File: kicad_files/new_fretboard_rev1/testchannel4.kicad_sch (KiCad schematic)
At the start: 22 parts, among them U2 LX3302AQPW-TR-EASY

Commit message: got 6 of em
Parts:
- removed C12, C13: 680pf, Capacitor_SMD:C_0603_1608Metric, symbol Device:C
- removed C14, C15: 10pf, Capacitor_SMD:C_0402_1005Metric, symbol Device:C
- removed C16: 1uf, Capacitor_SMD:C_0603_1608Metric, symbol Device:C
- removed C17, C20: 100nf, Capacitor_SMD:C_0402_1005Metric, symbol Device:C
- removed C18, C19: 6.8nf, Capacitor_SMD:C_0402_1005Metric, symbol Device:C
- removed C21: 1000pf, Capacitor_SMD:C_0402_1005Metric, symbol Device:C
- removed C22: 470nf, Capacitor_SMD:C_0402_1005Metric, symbol Device:C
- removed L5, L6, L7, L8: L, NetTie:NetTie-2_SMD_Pad0.5mm, symbol Device:L
- removed R10, R11, R8, R9: 10R, Resistor_SMD:R_0402_1005Metric, symbol Device:R
- removed R12: 221R, Resistor_SMD:R_0402_1005Metric, symbol Device:R
- removed R13: 4.7R, Resistor_SMD:R_0402_1005Metric, symbol Device:R
- removed U2: LX3302AQPW-TR-EASY, Snapeda:14-TSSOP_MCH-L, symbol Snapeda:LX3302AQPW-TR-EASY
- added C45, C51: 100nf, Capacitor_SMD:C_0402_1005Metric, symbol Device:C
- added C46: 1000pf, Capacitor_SMD:C_0402_1005Metric, symbol Device:C
- added C47: 470nf, Capacitor_SMD:C_0402_1005Metric, symbol Device:C
- added C48: 1uf, Capacitor_SMD:C_0603_1608Metric, symbol Device:C
- added C49, C50: 6.8nf, Capacitor_SMD:C_0402_1005Metric, symbol Device:C
- added C52, C53: 10pf, Capacitor_SMD:C_0402_1005Metric, symbol Device:C
- added C54, C55: 680pf, Capacitor_SMD:C_0603_1608Metric, symbol Device:C
- added L17, L18, L19, L20: L, NetTie:NetTie-2_SMD_Pad0.5mm, symbol Device:L
- added R25: 4.7R, Resistor_SMD:R_0402_1005Metric, symbol Device:R
- added R26: 221R, Resistor_SMD:R_0402_1005Metric, symbol Device:R
- added R27, R28, R29, R30: 10R, Resistor_SMD:R_0402_1005Metric, symbol Device:R
- added U5: LX3302AQPW-TR-EASY, Snapeda:14-TSSOP_MCH-L, symbol Snapeda:LX3302AQPW-TR-EASY
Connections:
- net CL1B_A: now also L20.1, R30.2
- net CL1_A: now also C52.1, R30.1, U5.8 (CL1)
- net CL2B_A: now also L19.1, R29.2
- net CL2_A: now also C53.1, R29.1, U5.10 (CL2)
- net GND: now also C45.1, C46.1, C47.1, C48.1, C49.1, C50.1, C52.2, C53.2, C54.2, C55.2, L19.2, L20.2, U5.2 (GND), U5.9 (GNDCL)
- net OSC11_A: now also C54.1, L17.2, U5.13 (OSC1)
- net OSC12_A: now also C55.1, L18.2, U5.12 (OSC2)
- net SUB_A: now also C51.1, U5.11 (SUB)
- net VIN_A: now also C46.2, C47.2, R25.1, R27.2, R28.1, U5.4 (VIN)
- new net: C48.2, C51.2, U5.5 (VDD)
- new net: C50.2, R26.1, R27.1, U5.6 (IO2)
- new net: C49.2, R26.2
- new net: C45.2, R25.2
- new net /OSC2B_A: L17.1, L18.1, R28.2
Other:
- removed sheet testchannel1
- removed sheet testchannel2
- removed sheet testchannel3
- removed sheet testchannel4
- removed sheet testchannel5

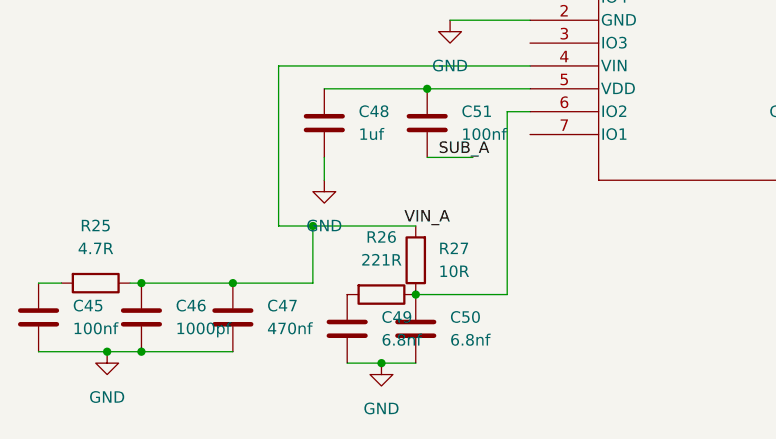
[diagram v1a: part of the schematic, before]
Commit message: stm32 micro added
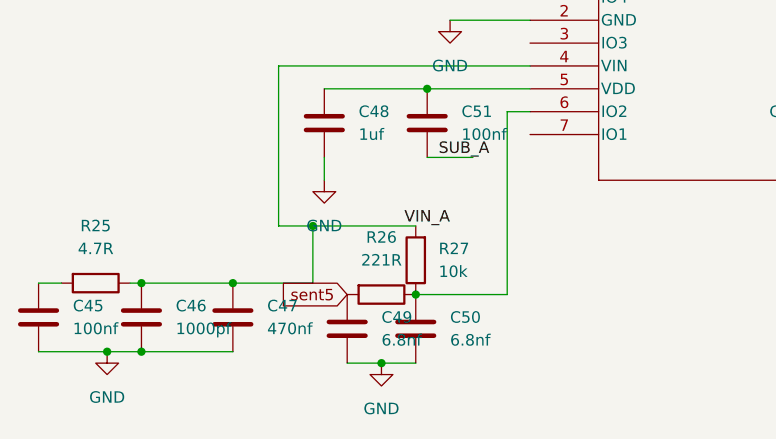
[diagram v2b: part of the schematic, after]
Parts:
- R27: value 10R -> 10k
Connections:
- net sent5: now reaches C49.2, R26.2
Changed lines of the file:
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@@
+		)
+	)
+	(global_label "sent5"
+		(shape input)
+		(at 87.63 125.73 180)
+		(fields_autoplaced yes)
+		(effects
+			(font
+				(size 1.27 1.27)
+			)
+			(justify right)
+		)
+		(property "Intersheetrefs" "${INTERSHEET_REFS}"
+			(at 79.4439 125.73 0)
+			(effects
+				(font
+					(size 1.27 1.27)
+				)
+				(justify right)
+				(hide yes)
+			)
 		)
 	)
@@
 			)
 		)
-		(property "Component Class" ""
-			(at 96.52 106.68 0)
-			(effects
-				(font
-					(size 1.27 1.27)
-				)
-				(hide yes)
-			)
-		)
 		(pin "1"
 		)
@@
 			)
 		)
-		(property "Component Class" ""
-			(at 171.45 68.58 0)
-			(effects
-				(font
-					(size 1.27 1.27)
-				)
-				(hide yes)
-			)
-		)
 		(pin "1"
 		)
@@
 			)
 		)
-		(property "Component Class" ""
-			(at 85.09 106.68 0)
-			(effects
-				(font
-					(size 1.27 1.27)
-				)
-				(hide yes)
-			)
-		)
 		(pin "1"
 		)
@@
 			)
 		)
-		(property "Component Class" ""
-			(at 91.44 125.73 90)
-			(effects
-				(font
-					(size 1.27 1.27)
-				)
-				(hide yes)
-			)
-		)
 		(pin "2"
 		)
@@
 			)
 		)
-		(property "Component Class" ""
-			(at 167.64 102.87 90)
-			(effects
-				(font
-					(size 1.27 1.27)
-				)
-				(hide yes)
-			)
-		)
 		(pin "1"
 		)
@@
 			)
 		)
-		(property "Component Class" ""
-			(at 180.34 121.92 90)
-			(effects
-				(font
-					(size 1.27 1.27)
-				)
-				(hide yes)
-			)
-		)
 		(pin "1"
 		)
@@
 			)
 		)
-		(property "Component Class" ""
-			(at 181.61 97.79 90)
-			(effects
-				(font
-					(size 1.27 1.27)
-				)
-				(hide yes)
-			)
-		)
 		(pin "1"
 		)
@@
 			)
 		)
-		(property "Component Class" ""
-			(at 95.25 129.54 0)
-			(effects
-				(font
-					(size 1.27 1.27)
-				)
-				(hide yes)
-			)
-		)
 		(pin "1"
 		)
@@
 			)
 		)
-		(property "Component Class" ""
-			(at 59.69 124.46 90)
-			(effects
-				(font
-					(size 1.27 1.27)
-				)
-				(hide yes)
-			)
-		)
 		(pin "2"
 		)
@@
 			)
 		)
-		(property "Component Class" ""
-			(at 74.93 128.27 0)
-			(effects
-				(font
-					(size 1.27 1.27)
-				)
-				(hide yes)
-			)
-		)
 		(pin "1"
 		)
@@
 			)
 		)
-		(property "Component Class" ""
-			(at 166.37 133.35 90)
-			(effects
-				(font
-					(size 1.27 1.27)
-				)
-				(hide yes)
-			)
-		)
 		(pin "1"
 		)
@@
 			)
 		)
-		(property "Component Class" ""
-			(at 107.95 92.71 0)
-			(effects
-				(font
-					(size 1.27 1.27)
-				)
-				(hide yes)
-			)
-		)
 		(pin "5"
 		)
@@
 			)
 		)
-		(property "Component Class" ""
-			(at 181.61 85.09 90)
-			(effects
-				(font
-					(size 1.27 1.27)
-				)
-				(hide yes)
-			)
-		)
 		(pin "1"
 		)
@@
 			)
 		)
-		(property "Component Class" ""
-			(at 64.77 128.27 0)
-			(effects
-				(font
-					(size 1.27 1.27)
-				)
-				(hide yes)
-			)
-		)
 		(pin "1"
 		)
@@
 			)
 		)
-		(property "Value" "10R"
+		(property "Value" "10k"
 			(at 97.79 123.1899 0)
 			(effects
@@
 			)
 		)
-		(property "Component Class" ""
-			(at 95.25 121.92 0)
-			(effects
-				(font
-					(size 1.27 1.27)
-				)
-				(hide yes)
-			)
-		)
 		(pin "2"
 		)
@@
 			)
 		)
-		(property "Component Class" ""
-			(at 167.64 113.03 90)
-			(effects
-				(font
-					(size 1.27 1.27)
-				)
-				(hide yes)
-			)
-		)
 		(pin "2"
 		)
@@
 			)
 		)
-		(property "Component Class" ""
-			(at 161.29 68.58 0)
-			(effects
-				(font
-					(size 1.27 1.27)
-				)
-				(hide yes)
-			)
-		)
 		(pin "1"
 		)
@@
 			)
 		)
-		(property "Component Class" ""
-			(at 168.91 121.92 90)
-			(effects
-				(font
-					(size 1.27 1.27)
-				)
-				(hide yes)
-			)
-		)
 		(pin "2"
 		)
@@
 			)
 		)
-		(property "Component Class" ""
-			(at 53.34 128.27 0)
-			(effects
-				(font
-					(size 1.27 1.27)
-				)
-				(hide yes)
-			)
-		)
 		(pin "1"
 		)
@@
 			)
 		)
-		(property "Component Class" ""
-			(at 180.34 113.03 90)
-			(effects
-				(font
-					(size 1.27 1.27)
-				)
-				(hide yes)
-			)
-		)
 		(pin "1"
 		)
@@
 			)
 		)
-		(property "Component Class" ""
-			(at 161.29 57.15 0)
-			(effects
-				(font
-					(size 1.27 1.27)
-				)
-				(hide yes)
-			)
-		)
 		(pin "2"
 		)
@@
 			(at 87.63 129.54 0)
 			(effects
-				(font
-					(size 1.27 1.27)
-				)
-				(hide yes)
-			)
-		)
-		(property "Component Class" ""
-			(at 87.63 129.54 0)
-			(effects

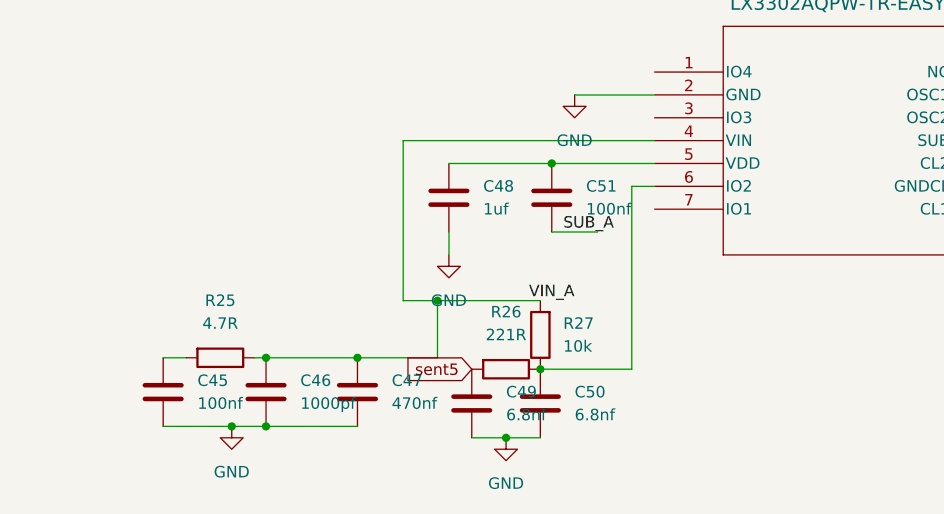
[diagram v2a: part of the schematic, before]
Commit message: mcu configured, still needs power connections and spi i2c connections
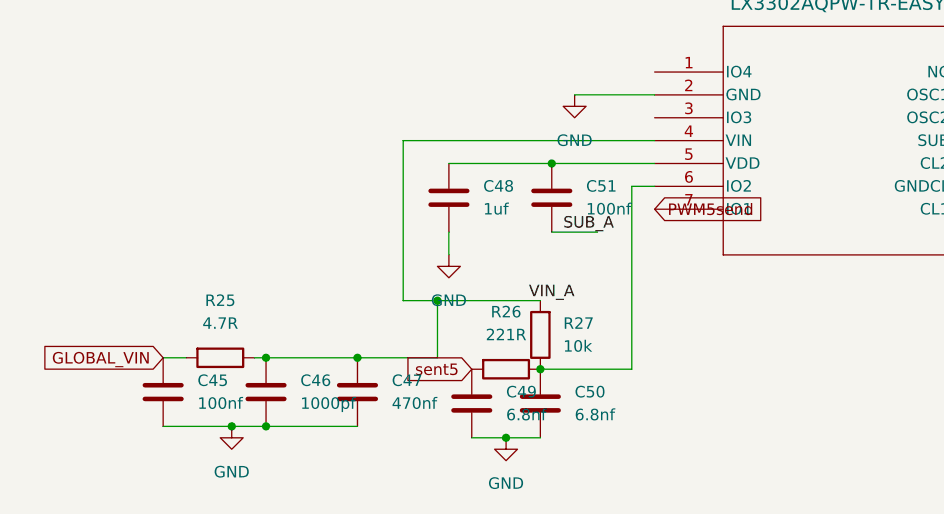
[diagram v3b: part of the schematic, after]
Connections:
- net GLOBAL_VIN: now reaches C45.2, R25.2
- net PWM5send: now reaches U5.7 (IO1)
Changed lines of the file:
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@@
+		)
+	)
+	(global_label "GLOBAL_VIN"
+		(shape input)
+		(at 53.34 124.46 180)
+		(fields_autoplaced yes)
+		(effects
+			(font
+				(size 1.27 1.27)
+			)
+			(justify right)
+		)
+		(property "Intersheetrefs" "${INTERSHEET_REFS}"
+			(at 39.348 124.46 0)
+			(effects
+				(font
+					(size 1.27 1.27)
+				)
+				(justify right)
+				(hide yes)
+			)
+		)
+	)
+	(global_label "PWM5send"
+		(shape input)
+		(at 107.95 107.95 0)
+		(fields_autoplaced yes)
+		(effects
+			(font
+				(size 1.27 1.27)
+			)
+			(justify left)
+		)
+		(property "Intersheetrefs" "${INTERSHEET_REFS}"
+			(at 120.7322 107.95 0)
+			(effects
+				(font
+					(size 1.27 1.27)
+				)
+				(justify left)
+				(hide yes)
+			)
 		)
 	)

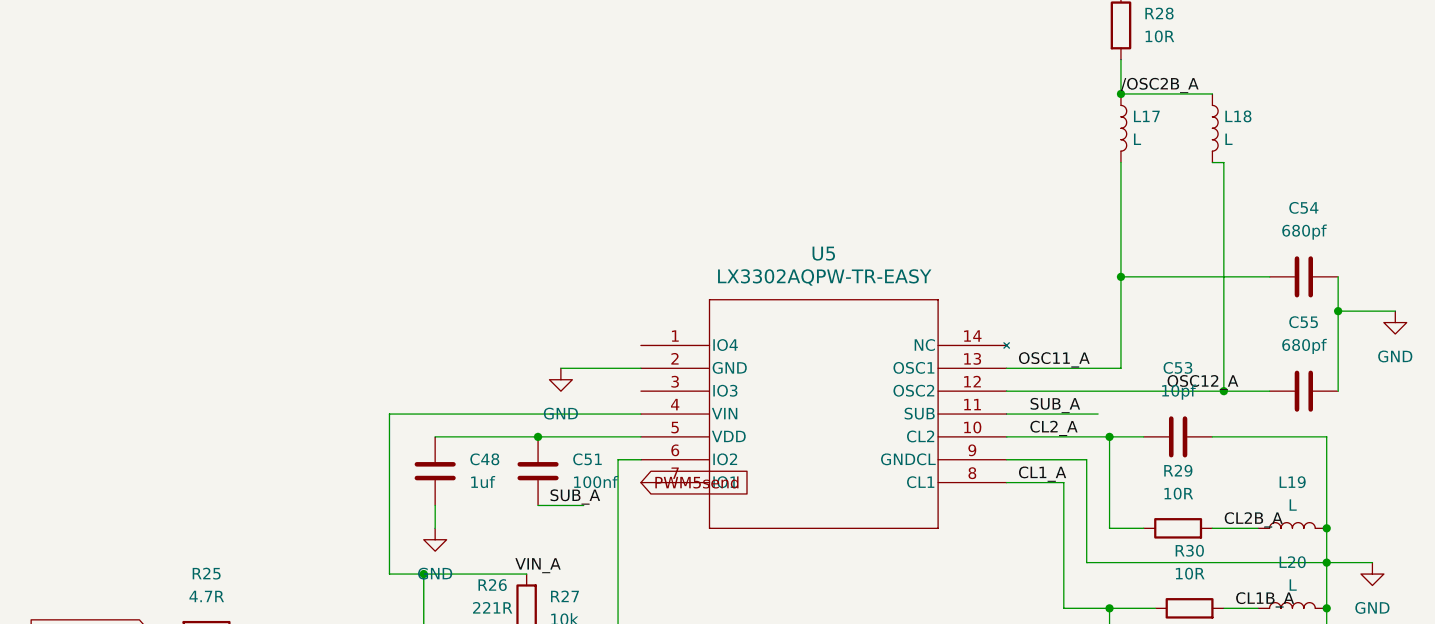
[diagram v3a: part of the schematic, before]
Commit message: finished routing - adding silkscreen
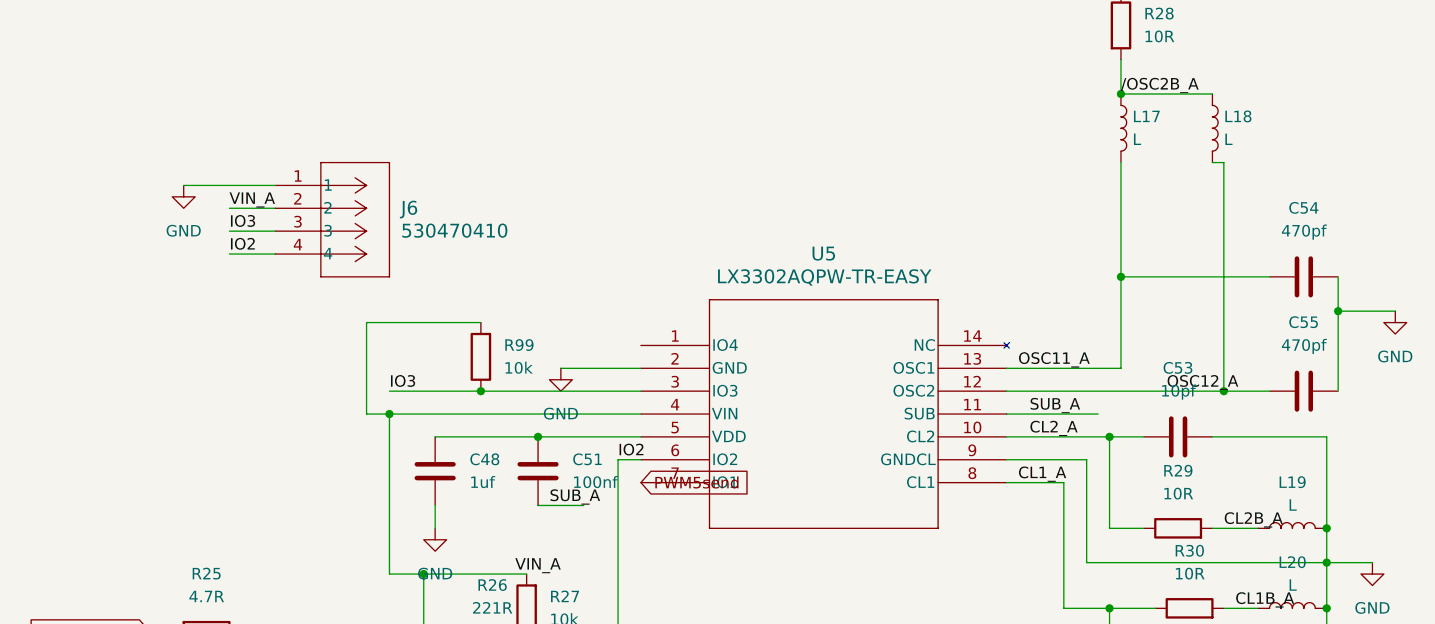
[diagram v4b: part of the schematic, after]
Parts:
- added J6: 530470410, Snapeda:CONN04_530470410_MOL, symbol Snapeda:530470410
- added R99: 10k, Resistor_SMD:R_0402_1005Metric, symbol Device:R
- C54, C55: value 680pf -> 470pf
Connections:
- net GND: now also J6.1
- net VIN_A: now also J6.2, R99.2
- net IO2: now reaches C50.2, R26.1, R27.1, U5.6 (IO2)
- net IO2: now also J6.4
- net IO3: now reaches U5.3 (IO3)
- net IO3: now also J6.3, R99.1

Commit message: exported gerbers of lefthand
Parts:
- L17, L18, L19, L20: now left out of the parts list
